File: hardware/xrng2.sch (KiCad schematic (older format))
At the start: 39 parts, among them J101 AVR-PDI-6A, J102 GS3, J103 GS3, J104 Conn_01x02, J105 Conn_01x03, J106 Conn_01x02, J107 USB_B, U101 CD4007, U102 XMEGA64A3U-A, U103 CD4007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

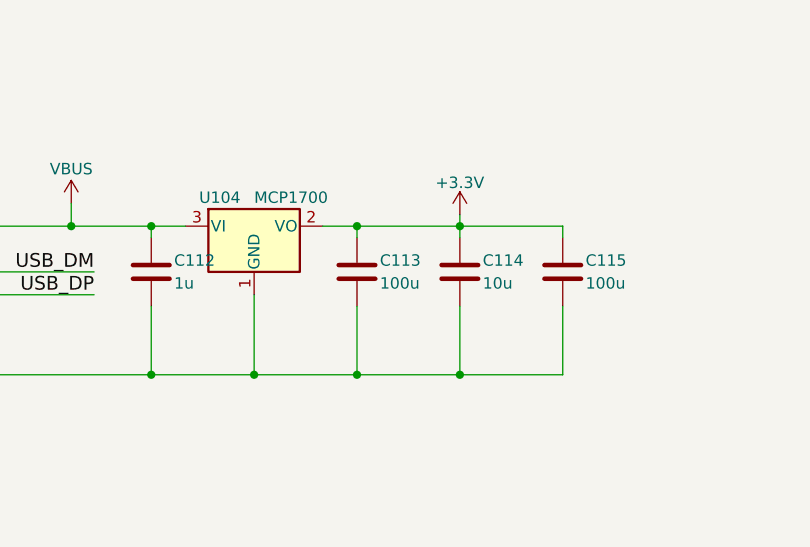
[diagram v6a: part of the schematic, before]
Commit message: Corrected C113 value
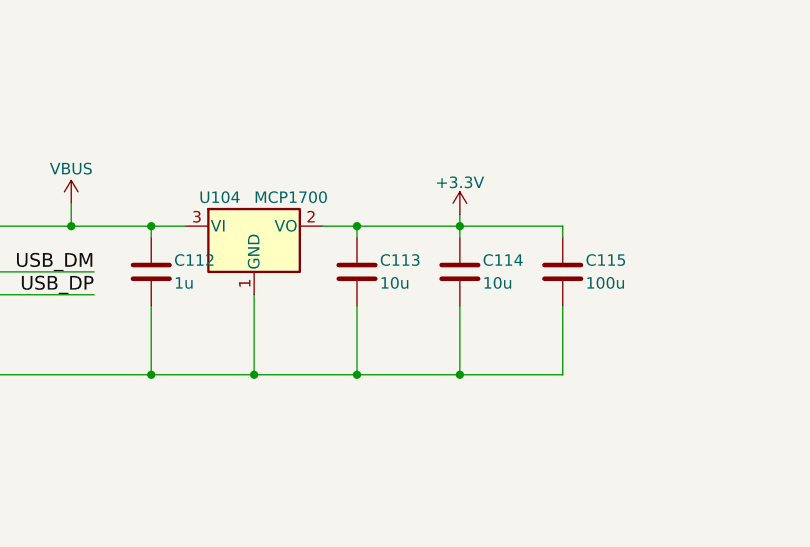
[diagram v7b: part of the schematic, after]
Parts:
- C113: value 100u -> 10u
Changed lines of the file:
@@
 P 5650 6400
 F 0 "C113" H 5750 6450 50  0000 L CNN
-F 1 "100u" H 5750 6350 50  0000 L CNN
+F 1 "10u" H 5750 6350 50  0000 L CNN
 F 2 "Capacitors_SMD:C_0603_HandSoldering" H 5688 6250 50  0001 C CNN
 F 3 "" H 5650 6400 50  0001 C CNN
